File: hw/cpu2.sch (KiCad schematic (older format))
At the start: 0 parts

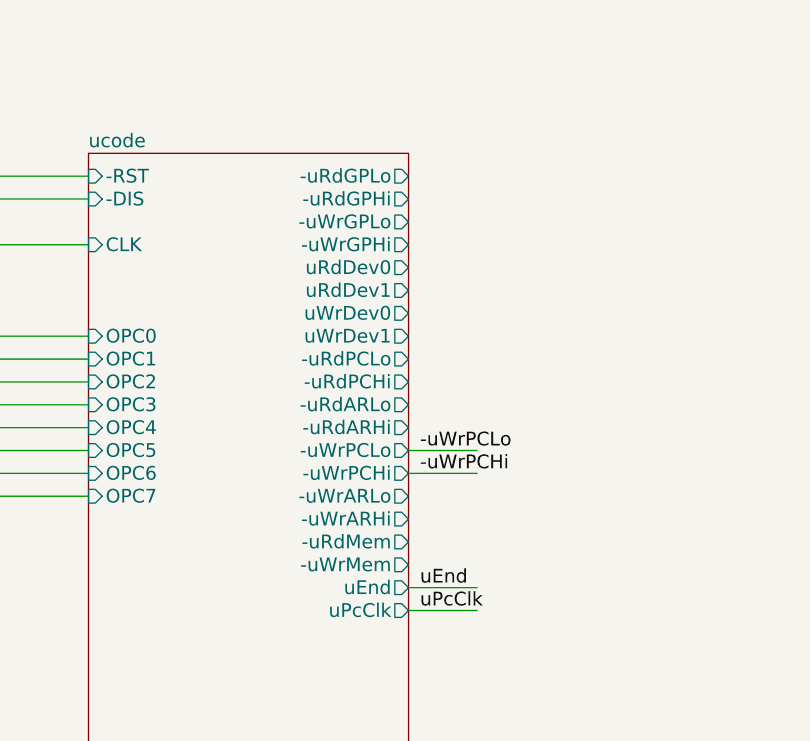
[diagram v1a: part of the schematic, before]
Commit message: redoing device read logic
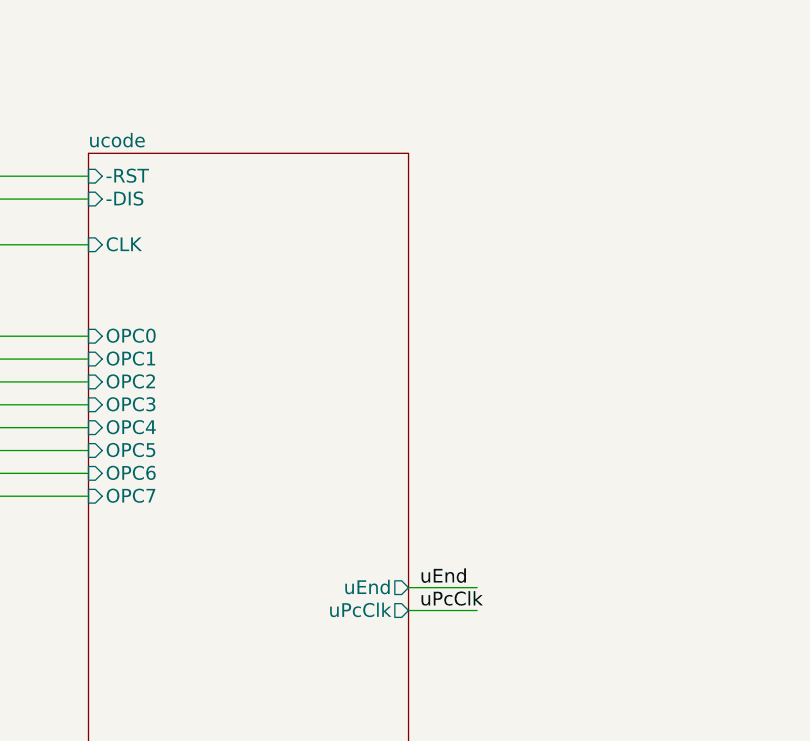
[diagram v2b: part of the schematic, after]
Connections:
- wire segments 120 -> 118
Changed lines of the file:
@@
-$EndSheet
-$Sheet
-S 7600 2050 1400 2700
-U 592C71D0
-F0 "ucode" 60
-F1 "ucode.sch" 60
-F2 "OPC0" I L 7600 2850 60
-F3 "OPC1" I L 7600 2950 60
-F4 "OPC2" I L 7600 3050 60
-F5 "OPC3" I L 7600 3150 60
-F6 "OPC4" I L 7600 3250 60
-F7 "OPC5" I L 7600 3350 60
-F8 "OPC6" I L 7600 3450 60
-F9 "OPC7" I L 7600 3550 60
-F10 "CLK" I L 7600 2450 60
-F11 "-uRdGPLo" O R 9000 2150 60
-F12 "-uRdGPHi" O R 9000 2250 60
-F13 "-uWrGPLo" O R 9000 2350 60
-F14 "-uWrGPHi" O R 9000 2450 60
-F15 "uRdDev0" O R 9000 2550 60
-F16 "uRdDev1" O R 9000 2650 60
-F17 "uWrDev0" O R 9000 2750 60
-F18 "uWrDev1" O R 9000 2850 60
-F19 "-uRdPCLo" O R 9000 2950 60
-F20 "-uRdPCHi" O R 9000 3050 60
-F21 "-uRdARLo" O R 9000 3150 60
-F22 "-uRdARHi" O R 9000 3250 60
-F23 "-uWrPCLo" O R 9000 3350 60
-F24 "-uWrPCHi" O R 9000 3450 60
-F25 "-uWrARLo" O R 9000 3550 60
-F26 "-uWrARHi" O R 9000 3650 60
-F27 "-uRdMem" O R 9000 3750 60
-F28 "-uWrMem" O R 9000 3850 60
-F29 "uEnd" O R 9000 3950 60
-F30 "uPcClk" O R 9000 4050 60
-F31 "-RST" I L 7600 2150 60
-F32 "-DIS" I L 7600 2250 60
 $EndSheet
 $Sheet
@@
 Text Label 4550 5600 0    60   ~ 0
 uPcClk
-Text Label 9050 3350 0    60   ~ 0
--uWrPCLo
-Text Label 9050 3450 0    60   ~ 0
--uWrPCHi
 Text Label 9050 4050 0    60   ~ 0
 uPcClk
@@
 	6200 3550 7600 3550
 Wire Wire Line
-	9000 3450 9300 3450
-Wire Wire Line
-	9000 3350 9300 3350
-Wire Wire Line
 	9000 4050 9300 4050
 Wire Wire Line
@@
 Entry Wire Line
 	9250 7500 9350 7600
+$Sheet
+S 7600 2050 1400 2700
+U 592C71D0
+F0 "ucode" 60
+F1 "ucode.sch" 60
+F2 "OPC0" I L 7600 2850 60
+F3 "OPC1" I L 7600 2950 60
+F4 "OPC2" I L 7600 3050 60
+F5 "OPC3" I L 7600 3150 60
+F6 "OPC4" I L 7600 3250 60
+F7 "OPC5" I L 7600 3350 60
+F8 "OPC6" I L 7600 3450 60
+F9 "OPC7" I L 7600 3550 60
+F10 "CLK" I L 7600 2450 60
+F11 "uEnd" O R 9000 3950 60
+F12 "uPcClk" O R 9000 4050 60
+F13 "-RST" I L 7600 2150 60
+F14 "-DIS" I L 7600 2250 60
+$EndSheet
 $EndSCHEMATC

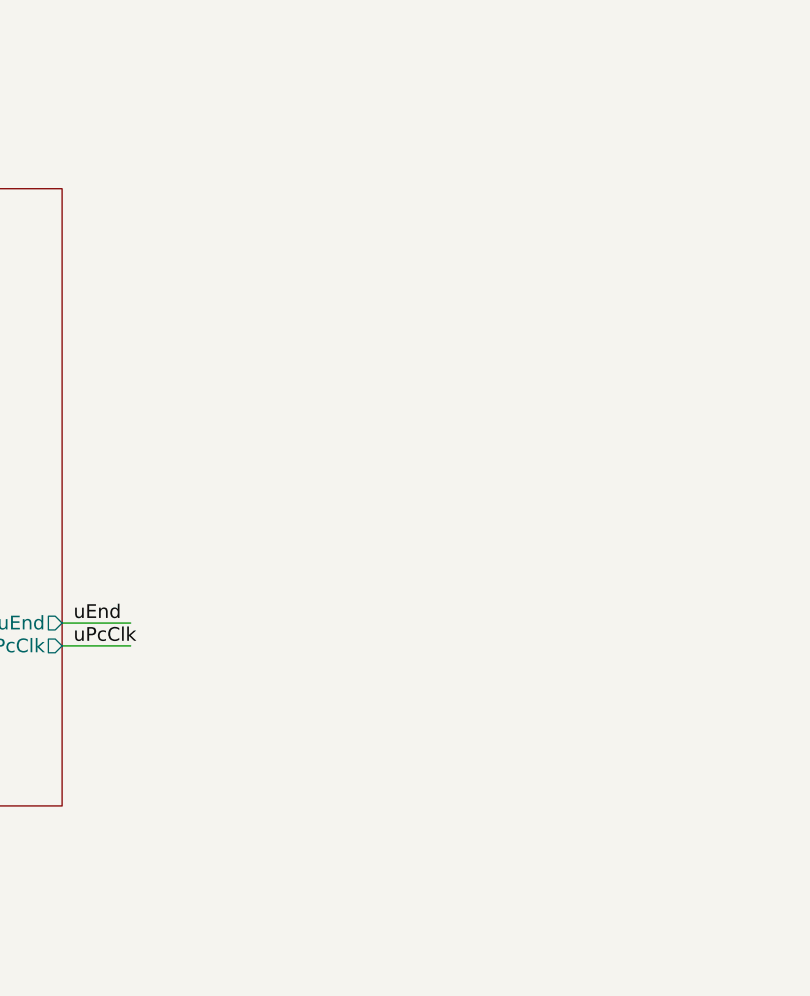
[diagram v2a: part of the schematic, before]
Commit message: microcode redesign
Rather than using logic to decode "packed" data
from the microcode, just use a 1:1 assignment of
microcode bits to control signals.  Since it looks
like 32 control signals will be sufficient, 4
microcode ROMs will do us.  Eliminating the
decoding logic reduces the chip count, and should
also result in better performance, since the
signals from the ROMs are clocked directly into
the '175 registers.
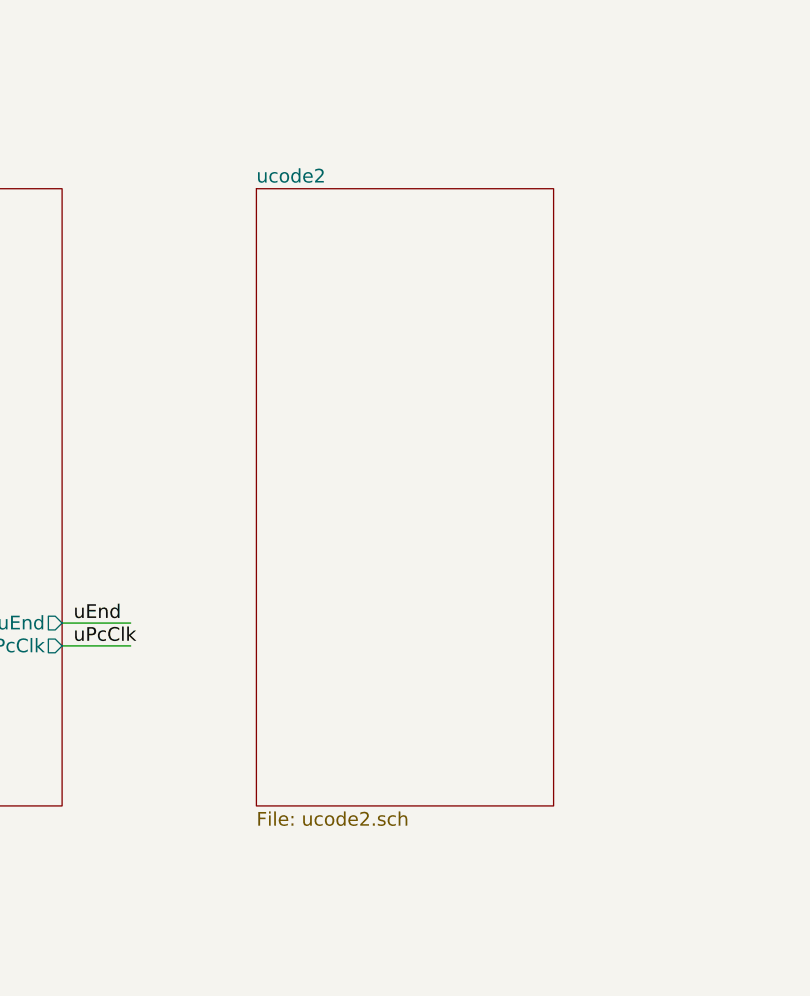
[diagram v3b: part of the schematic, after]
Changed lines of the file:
@@
 $Descr A3 16535 11693
 encoding utf-8
-Sheet 1 9
+Sheet 1 10
 Title ""
 Date ""
@@
 F14 "-DIS" I L 7600 2250 60
 $EndSheet
+$Sheet
+S 9850 2050 1300 2700
+U 594ECB9B
+F0 "ucode2" 60
+F1 "ucode2.sch" 60
+$EndSheet
 $EndSCHEMATC

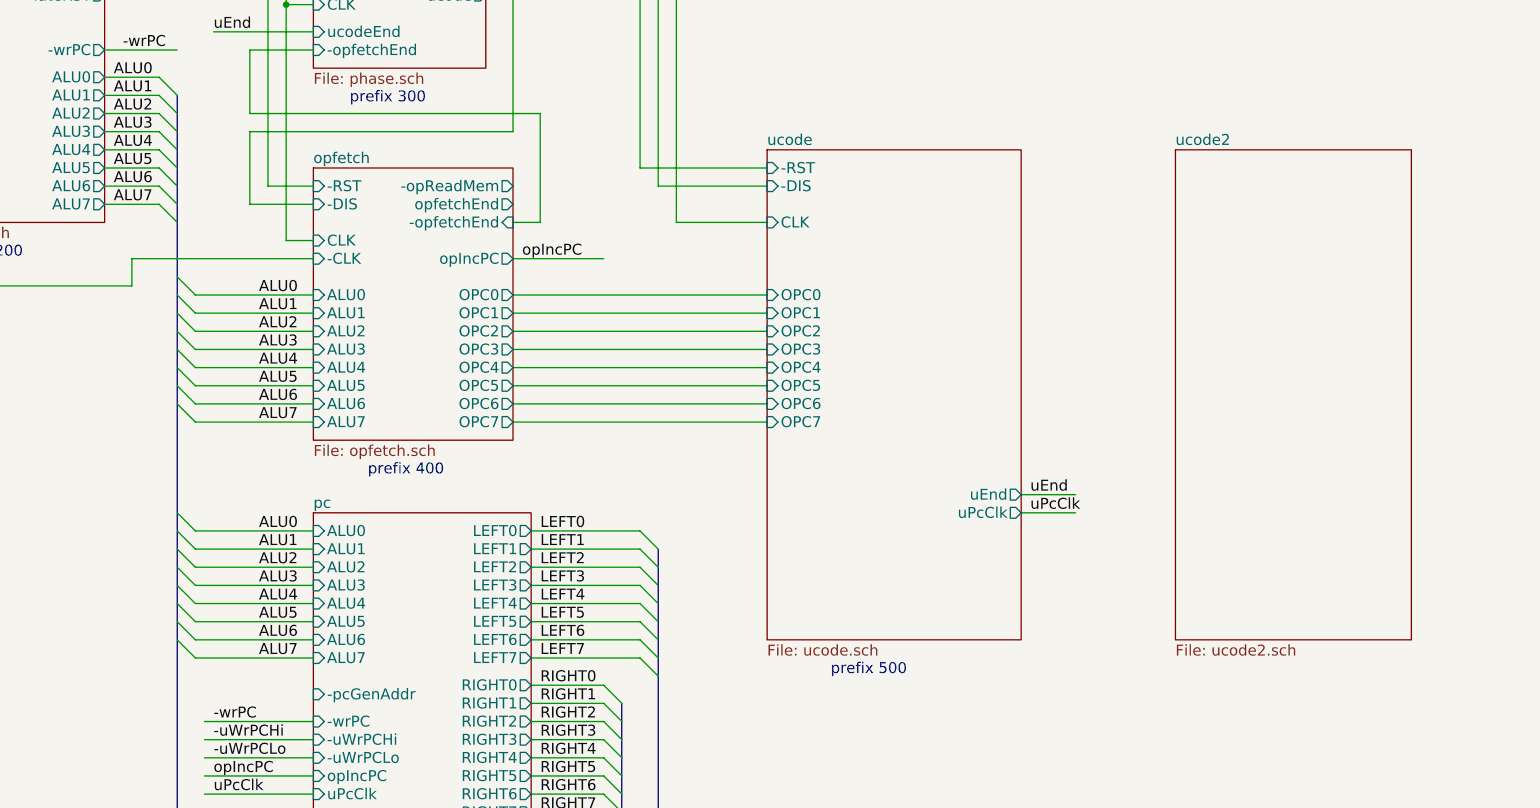
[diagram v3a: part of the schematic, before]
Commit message: switch over to ucode2 module for microcode
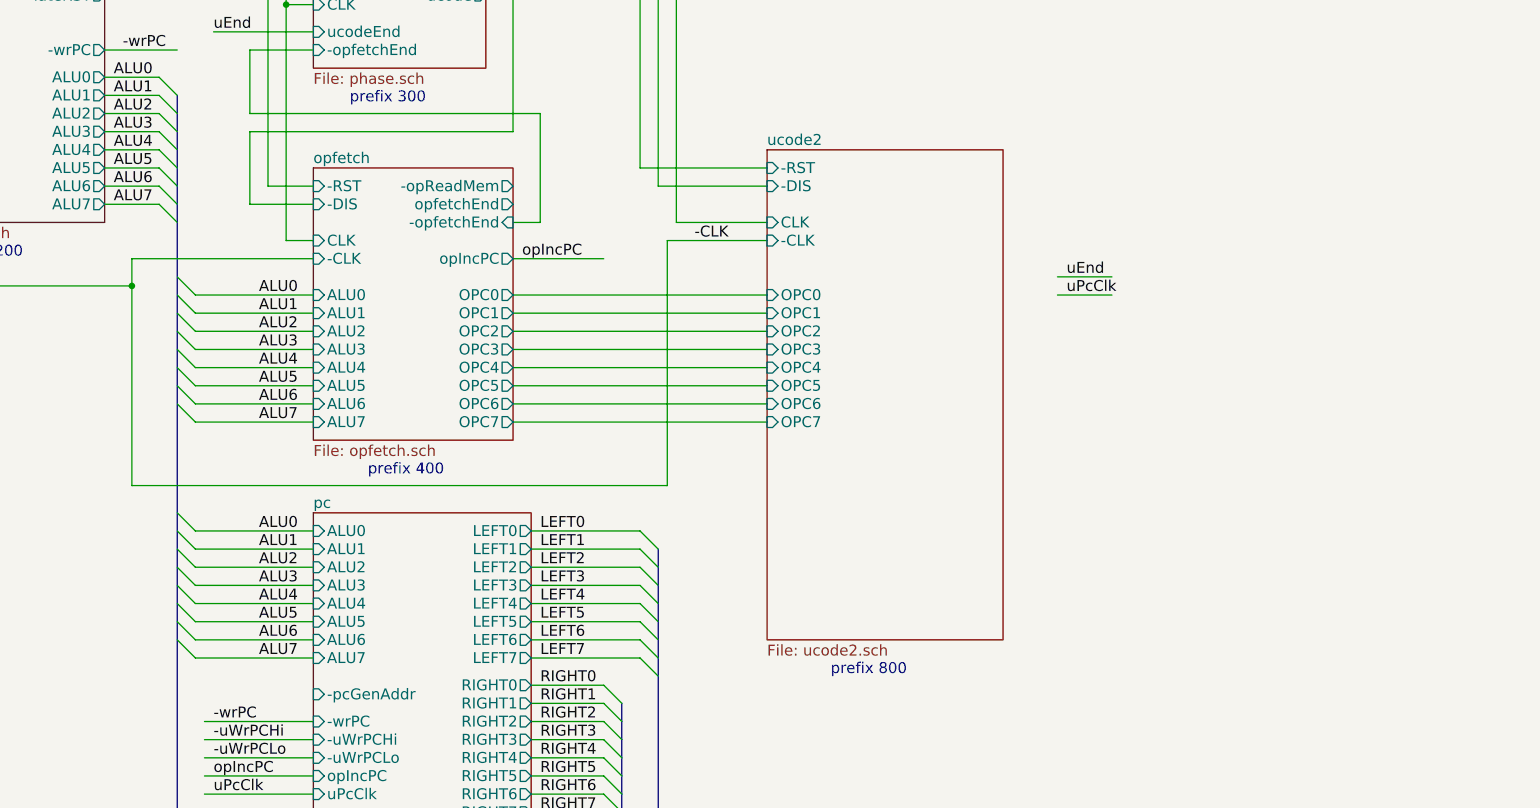
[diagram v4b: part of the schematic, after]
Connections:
- net labels added: -CLK
- wire segments 118 -> 121
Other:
- note added: "prefix 800"
- note removed: "prefix 500"
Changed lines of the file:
@@
 prefix 400
 Text Notes 7950 4950 0    60   ~ 0
-prefix 500
+prefix 800
 Text Notes 5400 5950 0    60   ~ 0
 prefix 600
@@
 Text Label 4550 5600 0    60   ~ 0
 uPcClk
-Text Label 9050 4050 0    60   ~ 0
+Text Label 9250 2850 0    60   ~ 0
 uPcClk
-Text Label 9050 3950 0    60   ~ 0
+Text Label 9250 2750 0    60   ~ 0
 uEnd
 Text Label 4550 1400 0    60   ~ 0
@@
 	5100 2650 4100 2650
 Wire Wire Line
-	4100 2650 4100 2800
+	4100 2650 4100 3900
 Wire Wire Line
 	4100 2800 2450 2800
@@
 	6200 3550 7600 3550
 Wire Wire Line
-	9000 4050 9300 4050
-Wire Wire Line
-	9000 3950 9300 3950
+	9200 2850 9500 2850
+Wire Wire Line
+	9200 2750 9500 2750
 Wire Wire Line
 	5100 1400 4550 1400
@@
 	9250 7500 9350 7600
 $Sheet
-S 7600 2050 1400 2700
-U 592C71D0
-F0 "ucode" 60
-F1 "ucode.sch" 60
+S 7600 2050 1300 2700
+U 594ECB9B
+F0 "ucode2" 60
+F1 "ucode2.sch" 60
 F2 "OPC0" I L 7600 2850 60
 F3 "OPC1" I L 7600 2950 60
@@
 F9 "OPC7" I L 7600 3550 60
 F10 "CLK" I L 7600 2450 60
-F11 "uEnd" O R 9000 3950 60
-F12 "uPcClk" O R 9000 4050 60
-F13 "-RST" I L 7600 2150 60
-F14 "-DIS" I L 7600 2250 60
+F11 "-RST" I L 7600 2150 60
+F12 "-DIS" I L 7600 2250 60
+F13 "-CLK" I L 7600 2550 60
 $EndSheet
-$Sheet
-S 9850 2050 1300 2700
-U 594ECB9B
-F0 "ucode2" 60
-F1 "ucode2.sch" 60
-$EndSheet
+Wire Wire Line
+	7050 2550 7600 2550
+Text Label 7200 2550 0    60   ~ 0
+-CLK
+Wire Wire Line
+	7050 2550 7050 3900
+Wire Wire Line
+	7050 3900 4100 3900
+Connection ~ 4100 2800
 $EndSCHEMATC

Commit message: use unused AND gate to allow 2 PC output enables
Both the opfetch logic and the microcode need to be
able to assert the contents of the PC onto the
left and right ALU input busses.
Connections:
- net labels added: -opReadMem
- wire segments 121 -> 123
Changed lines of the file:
@@
 F0 "pc" 60
 F1 "pc.sch" 60
-F2 "-pcGenAddr" I L 5100 5050 60
-F3 "ALU0" I L 5100 4150 60
-F4 "ALU1" I L 5100 4250 60
-F5 "ALU2" I L 5100 4350 60
-F6 "ALU3" I L 5100 4450 60
-F7 "ALU4" I L 5100 4550 60
-F8 "ALU5" I L 5100 4650 60
-F9 "ALU6" I L 5100 4750 60
-F10 "ALU7" I L 5100 4850 60
-F11 "LEFT0" O R 6300 4150 60
-F12 "LEFT1" O R 6300 4250 60
-F13 "LEFT2" O R 6300 4350 60
-F14 "LEFT3" O R 6300 4450 60
-F15 "LEFT4" O R 6300 4550 60
-F16 "LEFT5" O R 6300 4650 60
-F17 "LEFT6" O R 6300 4750 60
-F18 "LEFT7" O R 6300 4850 60
-F19 "RIGHT0" O R 6300 5000 60
-F20 "RIGHT1" O R 6300 5100 60
-F21 "RIGHT2" O R 6300 5200 60
-F22 "RIGHT3" O R 6300 5300 60
-F23 "RIGHT4" O R 6300 5400 60
-F24 "RIGHT5" O R 6300 5500 60
-F25 "RIGHT6" O R 6300 5600 60
-F26 "RIGHT7" O R 6300 5700 60
-F27 "-wrPC" I L 5100 5200 60
-F28 "-uWrPCHi" I L 5100 5300 60
-F29 "-uWrPCLo" I L 5100 5400 60
-F30 "opIncPC" I L 5100 5500 60
-F31 "uPcClk" I L 5100 5600 60
+F2 "ALU0" I L 5100 4150 60
+F3 "ALU1" I L 5100 4250 60
+F4 "ALU2" I L 5100 4350 60
+F5 "ALU3" I L 5100 4450 60
+F6 "ALU4" I L 5100 4550 60
+F7 "ALU5" I L 5100 4650 60
+F8 "ALU6" I L 5100 4750 60
+F9 "ALU7" I L 5100 4850 60
+F10 "LEFT0" O R 6300 4150 60
+F11 "LEFT1" O R 6300 4250 60
+F12 "LEFT2" O R 6300 4350 60
+F13 "LEFT3" O R 6300 4450 60
+F14 "LEFT4" O R 6300 4550 60
+F15 "LEFT5" O R 6300 4650 60
+F16 "LEFT6" O R 6300 4750 60
+F17 "LEFT7" O R 6300 4850 60
+F18 "RIGHT0" O R 6300 5000 60
+F19 "RIGHT1" O R 6300 5100 60
+F20 "RIGHT2" O R 6300 5200 60
+F21 "RIGHT3" O R 6300 5300 60
+F22 "RIGHT4" O R 6300 5400 60
+F23 "RIGHT5" O R 6300 5500 60
+F24 "RIGHT6" O R 6300 5600 60
+F25 "RIGHT7" O R 6300 5700 60
+F26 "-wrPC" I L 5100 5250 60
+F27 "-uWrPCHi" I L 5100 5350 60
+F28 "-uWrPCLo" I L 5100 5450 60
+F29 "opIncPC" I L 5100 5550 60
+F30 "uPcClk" I L 5100 5650 60
+F31 "-OE1" I L 5100 5050 60
+F32 "-OE2" I L 5100 5150 60
 $EndSheet
 $Sheet
@@
 Text Label 4050 1500 0    60   ~ 0
 -wrPC
-Text Label 4550 5200 0    60   ~ 0
+Text Label 4550 5250 0    60   ~ 0
 -wrPC
 Text Label 6250 2650 0    60   ~ 0
 opIncPC
-Text Label 4550 5500 0    60   ~ 0
+Text Label 4550 5550 0    60   ~ 0
 opIncPC
-Text Label 4550 5300 0    60   ~ 0
+Text Label 4550 5350 0    60   ~ 0
 -uWrPCHi
-Text Label 4550 5400 0    60   ~ 0
+Text Label 4550 5450 0    60   ~ 0
 -uWrPCLo
-Text Label 4550 5600 0    60   ~ 0
+Text Label 4550 5650 0    60   ~ 0
 uPcClk
 Text Label 9250 2850 0    60   ~ 0
@@
 	3950 1500 4350 1500
 Wire Wire Line
-	4500 5200 5100 5200
-Wire Wire Line
-	5100 5500 4500 5500
-Wire Wire Line
-	5100 5600 4500 5600
+	4500 5250 5100 5250
+Wire Wire Line
+	5100 5550 4500 5550
+Wire Wire Line
+	5100 5650 4500 5650
 Wire Wire Line
 	6200 2650 6700 2650
 Wire Wire Line
-	5100 5300 4500 5300
-Wire Wire Line
-	5100 5400 4500 5400
+	5100 5350 4500 5350
+Wire Wire Line
+	5100 5450 4500 5450
 Wire Wire Line
 	6050 1100 7000 1100
@@
 	7050 3900 4100 3900
 Connection ~ 4100 2800
+Wire Wire Line
+	6200 2250 6700 2250
+Text Label 6250 2250 0    60   ~ 0
+-opReadMem
+Wire Wire Line
+	5100 5050 4500 5050
+Text Label 4500 5050 0    60   ~ 0
+-opReadMem
 $EndSCHEMATC
